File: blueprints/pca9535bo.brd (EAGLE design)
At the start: 28.3 x 18.1 mm, 9 parts, among them IC1 PCA9535D, J1 0R, J2 0R, J3 0R

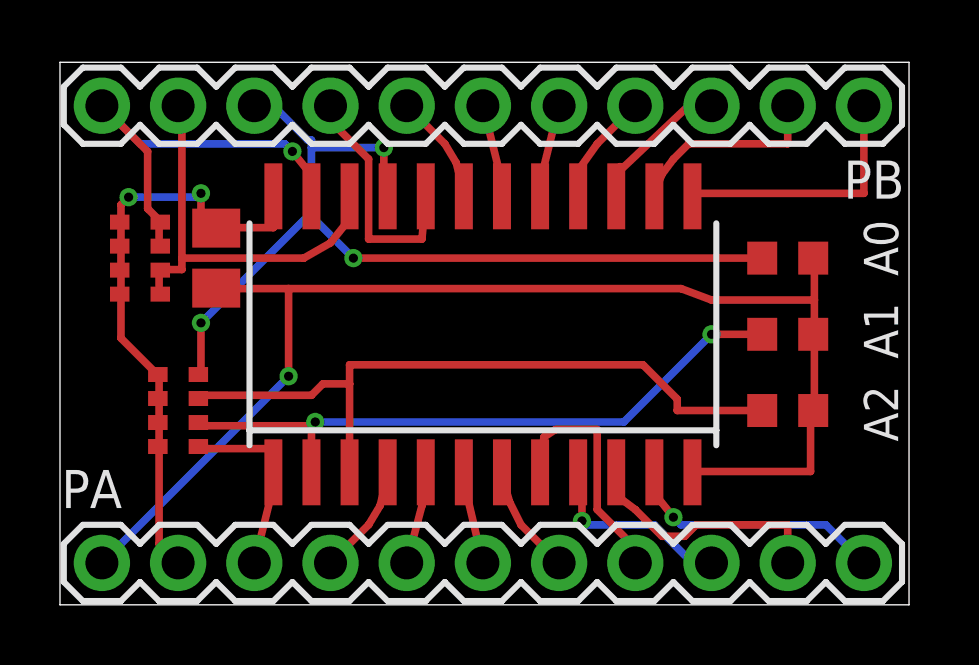
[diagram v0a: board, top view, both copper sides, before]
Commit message: GND polygon at bottom works
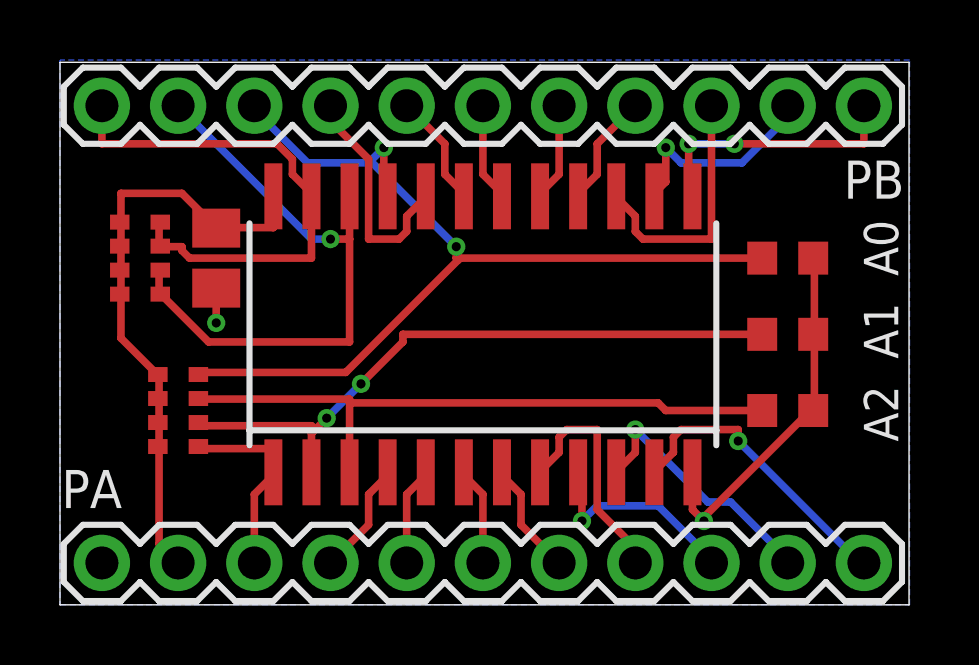
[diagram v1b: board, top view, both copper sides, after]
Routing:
- net GND: track 43.0 -> 13.4 mm, vias 1 -> 2
- net SCL: track 13.9 -> 20.2 mm, vias 0 -> 1
- net PB2: track 5.03 -> 8.52 mm
- net SDA: track 14.2 -> 17.5 mm, vias 1 -> 0
- net A2: track 23.4 -> 21.3 mm
- net PA7: track 8.67 -> 9.95 mm
- net A0: track 31.5 -> 32.0 mm, vias 3 -> 2
- net PB1: track 6.71 -> 7.07 mm, vias 0 -> 1
- net PA6: track 8.38 -> 8.68 mm, vias 0 -> 1
- net PB0: track 8.73 -> 8.91 mm, vias 0 -> 2
- net 5V: track 20.1 -> 19.9 mm, vias 2 -> 0
- added copper zone on layer 16, net GND

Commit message: cleaned up
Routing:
- net SCL: track 20.2 -> 21.1 mm
- net PA6: track 8.68 -> 9.45 mm
